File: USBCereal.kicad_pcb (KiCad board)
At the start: 2 copper layers, 24.3 x 19.6 mm, 14 parts, among them J1 USB_C, J2 Conn_01x06, U1 XC6206P332MR, U2 CH340C

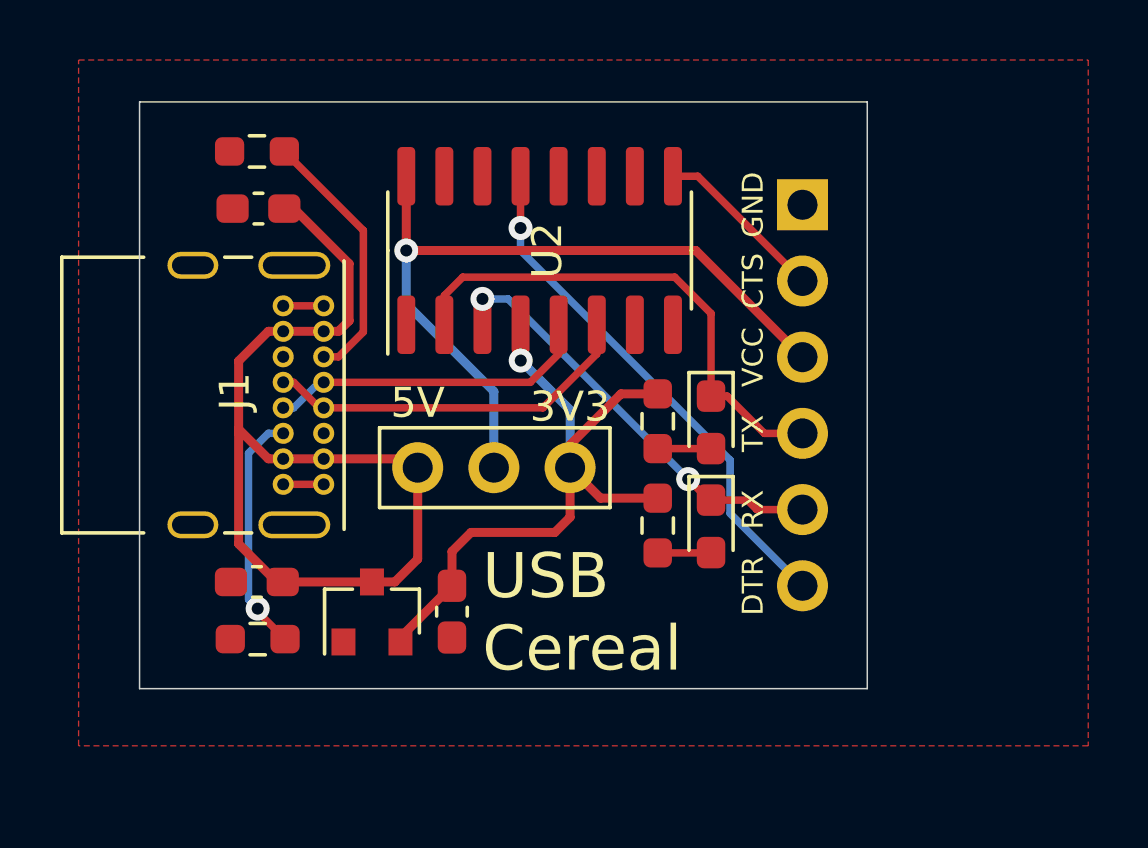
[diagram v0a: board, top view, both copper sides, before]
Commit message: update schematic
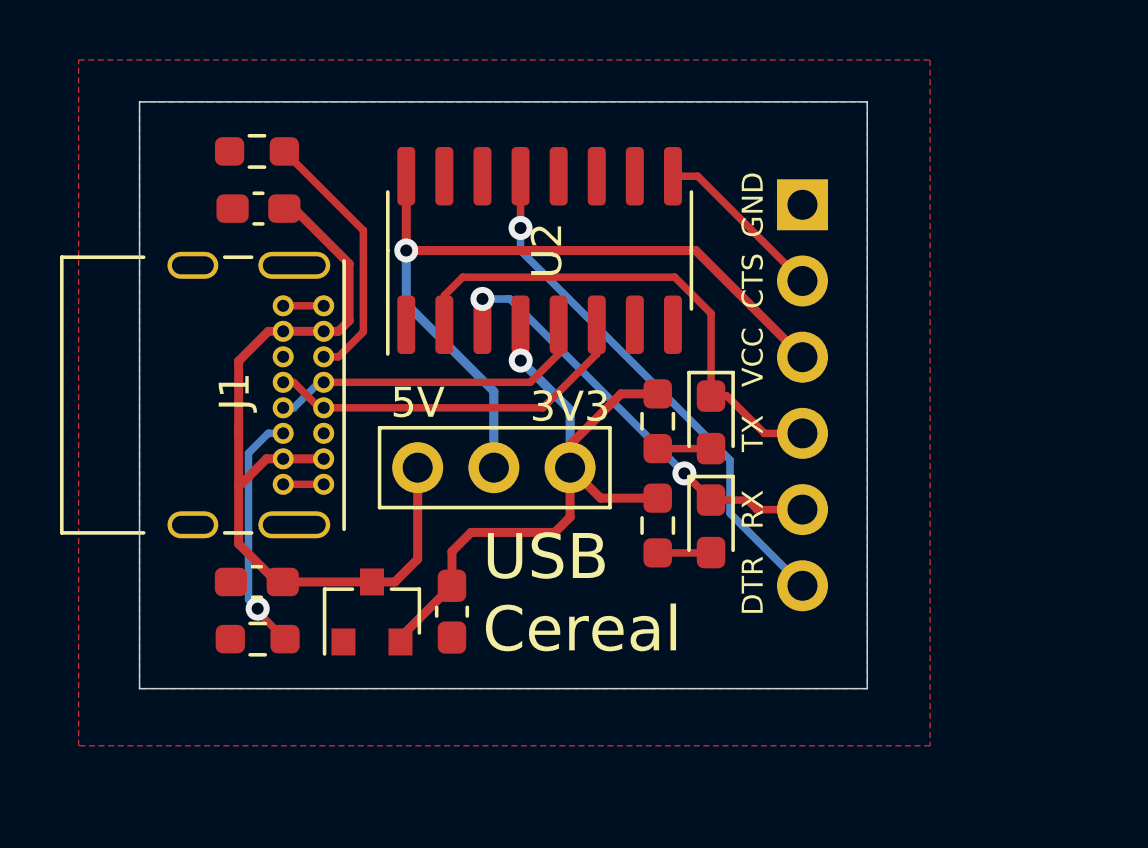
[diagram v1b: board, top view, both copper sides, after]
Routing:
- net +5V: track 31.8 -> 29.0 mm
- added copper zone on B.Cu, net GNDD
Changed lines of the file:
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@@
     (thickness 1.6)
     (drawings 13)
-    (tracks 100)
+    (tracks 102)
     (zones 0)
     (modules 14)
@@
       (effects (font (size 1 1) (thickness 0.15)))
     )
-    (fp_text user %R (at 0 0 90) (layer F.Fab)
-      (effects (font (size 0.4 0.4) (thickness 0.06)))
-    )
     (fp_line (start 0.8 -0.4) (end -0.5 -0.4) (layer F.Fab) (width 0.1))
     (fp_line (start -0.5 -0.4) (end -0.8 -0.1) (layer F.Fab) (width 0.1))
@@
     (fp_line (start 1.65 -0.73) (end 1.65 0.73) (layer F.CrtYd) (width 0.05))
     (fp_line (start 1.65 0.73) (end -1.65 0.73) (layer F.CrtYd) (width 0.05))
+    (fp_text user %R (at 0 0 90) (layer F.Fab)
+      (effects (font (size 0.4 0.4) (thickness 0.06)))
+    )
     (pad 2 smd roundrect (at 0.875 0 270) (size 1.05 0.95) (layers F.Cu F.Paste F.Mask) (roundrect_rratio 0.25)
       (net 13 "Net-(D1-Pad2)"))
@@
     (fp_text value LED_Small (at 4.6485 -0.127 90) (layer F.Fab) hide
       (effects (font (size 1 1) (thickness 0.15)))
-    )
-    (fp_text user %R (at 0 0 90) (layer F.Fab)
-      (effects (font (size 0.4 0.4) (thickness 0.06)))
     )
     (fp_line (start 0.8 -0.4) (end -0.5 -0.4) (layer F.Fab) (width 0.1))
@@
     (fp_line (start 1.65 -0.73) (end 1.65 0.73) (layer F.CrtYd) (width 0.05))
     (fp_line (start 1.65 0.73) (end -1.65 0.73) (layer F.CrtYd) (width 0.05))
+    (fp_text user %R (at 0 0 90) (layer F.Fab)
+      (effects (font (size 0.4 0.4) (thickness 0.06)))
+    )
     (pad 2 smd roundrect (at 0.875 0 270) (size 1.05 0.95) (layers F.Cu F.Paste F.Mask) (roundrect_rratio 0.25)
       (net 14 "Net-(D2-Pad2)"))
@@
     (effects (font (size 0.7 0.7) (thickness 0.1)))
   )
-  (gr_text "USB\nCereal" (at 32.512 34.29) (layer F.SilkS)
+  (gr_text "USB\nCereal" (at 32.512 33.655) (layer F.SilkS)
     (effects (font (size 1.5 1.5) (thickness 0.375)) (justify left))
   )
@@
   (gr_line (start 21.082 36.83) (end 21.082 17.272) (layer Edge.Cuts) (width 0.05))
   (segment (start 25.87 24.919) (end 27.22 24.919) (width 0.3) (layer F.Cu) (net 1))
-  (segment (start 25.375026 29.169) (end 25.87 29.169) (width 0.3) (layer F.Cu) (net 1))
-  (segment (start 24.384 28.177974) (end 25.375026 29.169) (width 0.3) (layer F.Cu) (net 1))
   (segment (start 25.87 29.169) (end 27.22 29.169) (width 0.3) (layer F.Cu) (net 1))
   (segment (start 25.654 33.274) (end 25.855 33.274) (width 0.3) (layer F.Cu) (net 1))
@@
   (segment (start 24.384 25.910026) (end 24.384 28.321) (width 0.3) (layer F.Cu) (net 1))
   (segment (start 25.87 24.919) (end 25.375026 24.919) (width 0.3) (layer F.Cu) (net 1))
-  (segment (start 24.384 28.321) (end 24.384 32.004) (width 0.3) (layer F.Cu) (net 1))
   (segment (start 25.375026 24.919) (end 24.384 25.910026) (width 0.3) (layer F.Cu) (net 1))
   (segment (start 24.384 28.177974) (end 24.384 28.321) (width 0.3) (layer F.Cu) (net 1))
@@
   (segment (start 28.067 24.566974) (end 28.067 22.664616) (width 0.3) (layer F.Cu) (net 1))
   (segment (start 30.058 29.169) (end 30.353 29.464) (width 0.3) (layer F.Cu) (net 1))
-  (segment (start 27.22 29.169) (end 30.058 29.169) (width 0.3) (layer F.Cu) (net 1))
   (segment (start 25.966 33.163) (end 25.855 33.274) (width 0.3) (layer F.Cu) (net 1))
   (segment (start 25.855 33.274) (end 28.829 33.274) (width 0.3) (layer F.Cu) (net 1))
@@
   (segment (start 30.353 32.512) (end 30.353 29.464) (width 0.3) (layer F.Cu) (net 1))
   (segment (start 29.591 33.274) (end 30.353 32.512) (width 0.3) (layer F.Cu) (net 1))
+  (segment (start 25.314 29.169) (end 24.384 30.099) (width 0.3) (layer F.Cu) (net 1))
+  (segment (start 24.384 30.099) (end 24.384 32.004) (width 0.3) (layer F.Cu) (net 1))
+  (segment (start 25.87 29.169) (end 25.314 29.169) (width 0.3) (layer F.Cu) (net 1))
+  (segment (start 24.384 28.321) (end 24.384 30.099) (width 0.3) (layer F.Cu) (net 1))
   (segment (start 25.87 30.019) (end 27.22 30.019) (width 0.25) (layer F.Cu) (net 4))
   (segment (start 25.87 24.069) (end 27.22 24.069) (width 0.25) (layer F.Cu) (net 4))
@@
   (segment (start 41.656 30.861) (end 43.18 30.861) (width 0.25) (layer F.Cu) (net 11))
   (segment (start 41.3395 30.5445) (end 41.656 30.861) (width 0.25) (layer F.Cu) (net 11))
-  (via (at 39.37 29.845) (size 0.8) (drill 0.4) (layers F.Cu B.Cu) (net 11))
-  (segment (start 40.0695 30.5445) (end 39.37 29.845) (width 0.25) (layer F.Cu) (net 11))
+  (via (at 39.243 29.6545) (size 0.8) (drill 0.4) (layers F.Cu B.Cu) (net 11))
   (segment (start 40.132 30.5445) (end 40.0695 30.5445) (width 0.25) (layer F.Cu) (net 11))
   (via (at 32.512 23.839) (size 0.8) (drill 0.4) (layers F.Cu B.Cu) (net 11))
   (segment (start 33.364 23.839) (end 32.512 23.839) (width 0.25) (layer B.Cu) (net 11))
-  (segment (start 39.37 29.845) (end 33.364 23.839) (width 0.25) (layer B.Cu) (net 11))
+  (segment (start 40.132 30.5435) (end 39.243 29.6545) (width 0.25) (layer F.Cu) (net 11))
+  (segment (start 40.132 30.5445) (end 40.132 30.5435) (width 0.25) (layer F.Cu) (net 11))
+  (segment (start 33.4275 23.839) (end 33.364 23.839) (width 0.25) (layer B.Cu) (net 11))
+  (segment (start 39.243 29.6545) (end 33.4275 23.839) (width 0.25) (layer B.Cu) (net 11))
   (segment (start 40.132 27.079) (end 40.668 27.079) (width 0.25) (layer F.Cu) (net 12))
   (segment (start 41.91 28.321) (end 43.18 28.321) (width 0.25) (layer F.Cu) (net 12))
@@
     (connect_pads (clearance 0.0254))
     (min_thickness 0.254)
-    (fill yes (arc_segments 32) (thermal_gap 0.508) (thermal_bridge_width 0.508))
+    (fill yes (arc_segments 32) (thermal_gap 0.3) (thermal_bridge_width 0.3))
     (polygon
       (pts
-        (xy 52.705 38.735) (xy 19.05 38.735) (xy 19.05 15.875) (xy 52.705 15.875)
+        (xy 47.4345 38.735) (xy 19.05 38.735) (xy 19.05 15.875) (xy 47.4345 15.875)
       )
     )
+  )
+  (zone (net 4) (net_name GNDD) (layer B.Cu) (hatch edge 0.508)
+    (connect_pads (clearance 0.0254))
+    (min_thickness 0.254)
+    (fill yes (arc_segments 32) (thermal_gap 0.3) (thermal_bridge_width 0.3))
+    (polygon
+      (pts
+        (xy 45.339 36.83) (xy 21.082 36.83) (xy 21.082 17.272) (xy 45.339 17.272)
+      )
+    )
+  )
+  (zone (net 0) (net_name "") (layer B.Cu) (hatch edge 0.508)
+    (connect_pads (clearance 0.0254))
+    (min_thickness 0.254)
+    (keepout (tracks allowed) (vias allowed) (copperpour not_allowed))
+    (fill (arc_segments 32) (thermal_gap 0.508) (thermal_bridge_width 0.508))
+    (polygon
+      (pts
+        (xy 27.178 30.48) (xy 25.019 30.48) (xy 25.019 28.956) (xy 27.178 28.956)
+      )
+    )
+  )
+  (zone (net 0) (net_name "") (layer F.Cu) (hatch edge 0.508)
+    (connect_pads (clearance 0.0254))
+    (min_thickness 0.254)
+    (keepout (tracks allowed) (vias allowed) (copperpour not_allowed))
+    (fill (arc_segments 32) (thermal_gap 0.508) (thermal_bridge_width 0.508))
+    (polygon
+      (pts
+        (xy 31.877 22.86) (xy 30.988 23.6855) (xy 30.6705 23.6855) (xy 30.1625 23.495) (xy 30.1625 22.5425)
+        (xy 31.877 22.5425)
+      )
+    )
+  )
+  (zone (net 0) (net_name "") (layer F.Cu) (hatch edge 0.508)
+    (connect_pads (clearance 0.0254))
+    (min_thickness 0.254)
+    (keepout (tracks allowed) (vias allowed) (copperpour not_allowed))
+    (fill (arc_segments 32) (thermal_gap 0.508) (thermal_bridge_width 0.508))
+    (polygon
+      (pts
+        (xy 30.48 26.3525) (xy 27.7495 26.3525) (xy 27.7495 25.9715) (xy 28.829 24.892) (xy 30.48 24.892)
+      )
+    )
+  )
+  (zone (net 0) (net_name "") (layer B.Cu) (hatch edge 0.508)
+    (connect_pads (clearance 0.0254))
+    (min_thickness 0.254)
+    (keepout (tracks allowed) (vias allowed) (copperpour not_allowed))
+    (fill (arc_segments 32) (thermal_gap 0.3) (thermal_bridge_width 0.3))
+    (polygon
+      (pts
+        (xy 27.1145 24.1935) (xy 25.908 24.1935) (xy 25.908 23.241) (xy 27.1145 23.241)
+      )
+    )
+  )
+  (zone (net 0) (net_name "") (layer F.Cu) (hatch edge 0.508)
+    (connect_pads (clearance 0.0254))
+    (min_thickness 0.254)
+    (keepout (tracks allowed) (vias allowed) (copperpour not_allowed))
+    (fill (arc_segments 32) (thermal_gap 0.3) (thermal_bridge_width 0.3))
+    (polygon
+      (pts
+        (xy 27.2415 30.861) (xy 24.8285 30.861) (xy 24.8285 29.9085) (xy 27.2415 29.9085)
+      )
+    )
+  )
+  (zone (net 0) (net_name "") (layer F.Cu) (hatch edge 0.508)
+    (connect_pads (clearance 0.0254))
+    (min_thickness 0.254)
+    (keepout (tracks allowed) (vias allowed) (copperpour not_allowed))
+    (fill (arc_segments 32) (thermal_gap 0.3) (thermal_bridge_width 0.3))
+    (polygon
+      (pts
+        (xy 27.3685 24.257) (xy 25.9715 24.257) (xy 25.9715 23.368) (xy 27.3685 23.368)
+      )
+    )

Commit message: Add logo
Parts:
- added G***: LOGO, USBCereal:USBCereal, B.Cu at (37.4, 23.6)

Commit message: Finished PCB, generated fabrication files
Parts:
- added REF**: JLCPCB_Tooling_Hole, USBCereal:JLCPCB_Tooling_Hole, F.Cu at (45.3, 27.1)
- added REF**: JLCPCB_Tooling_Hole, USBCereal:JLCPCB_Tooling_Hole, F.Cu at (22.0, 34.2)
- added REF**: JLCPCB_Tooling_Hole, USBCereal:JLCPCB_Tooling_Hole, F.Cu at (22.0, 19.9)
- J1: footprint Connector_USB:USB_C_Receptacle_GCT_USB4085 -> Connector_USB:USB_C_Receptacle_HRO_TYPE-C-31-M-12
- R3, R4: value 51 -> 47R
- moved J1 4.58 mm to (23.7, 27.1)
- moved R2 1.91 mm to (25.1, 20.8)
- moved R1 1.88 mm to (25.1, 33.3)
- moved C2 1.78 mm to (25.1, 35.1)
- moved C1 1.78 mm to (25.1, 19.1)
- moved G*** 1.76 mm to (35.8, 22.9)
- moved D1 0.76 mm to (40.9, 28.0)
- moved D2 0.76 mm to (40.9, 31.4)
- moved R3 0.76 mm to (39.1, 27.9)
- moved R4 0.76 mm to (39.1, 31.4)
- moved U2 0.76 mm to (35.2, 22.2)
- moved JP1 0.76 mm to (31.1, 29.5)
- moved C3 0.13 mm to (31.6, 34.3)
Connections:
- J1 pad A8: Net-(J1-PadA8) -> (no net)
- J1 pad B8: Net-(J1-PadB8) -> (no net)
- U2 pad 10: Net-(U2-Pad10) -> (no net)
- U2 pad 11: Net-(U2-Pad11) -> (no net)
- U2 pad 12: Net-(U2-Pad12) -> (no net)
- U2 pad 14: Net-(U2-Pad14) -> (no net)
- U2 pad 15: Net-(U2-Pad15) -> (no net)
- U2 pad 7: Net-(U2-Pad7) -> (no net)
- U2 pad 8: Net-(U2-Pad8) -> (no net)
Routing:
- net /USB_D-: track 12.5 -> 16.2 mm, vias 0 -> 2
- net /USB_D+: track 10.9 -> 13.0 mm
- net /CC1: track 8.77 -> 6.78 mm
- net +5V: track 29.0 -> 27.1 mm, vias 0 -> 3
- net /CC2: track 8.13 -> 6.42 mm, vias 1 -> 0
- net GNDD: track 2.70 -> 4.34 mm, vias 0 -> 8
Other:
- board size 24.3 x 19.6 mm -> 25.1 x 19.6 mm
- net class VCC: trace_width 0.3 -> 0.5
- board text added: "JLCJLCJLCJLC"

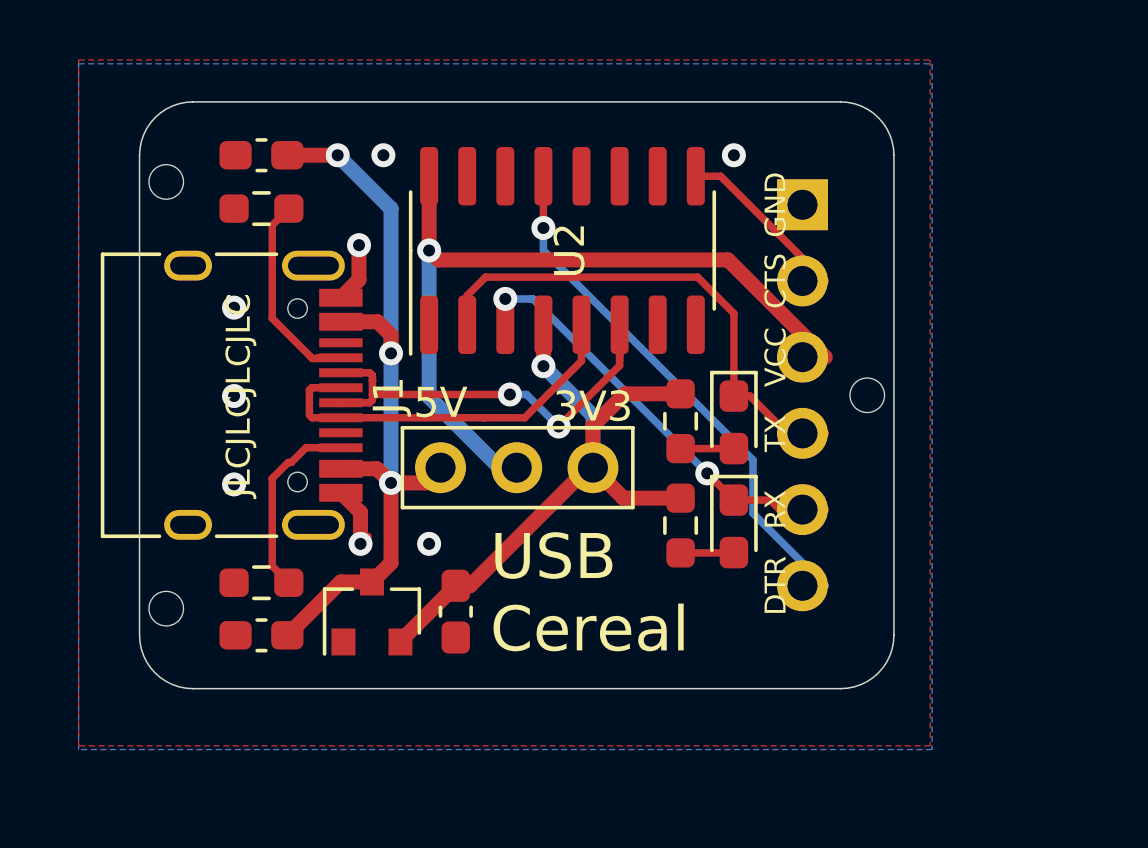
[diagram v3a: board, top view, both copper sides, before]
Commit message: update non-connecting traces, rebuild gerber's
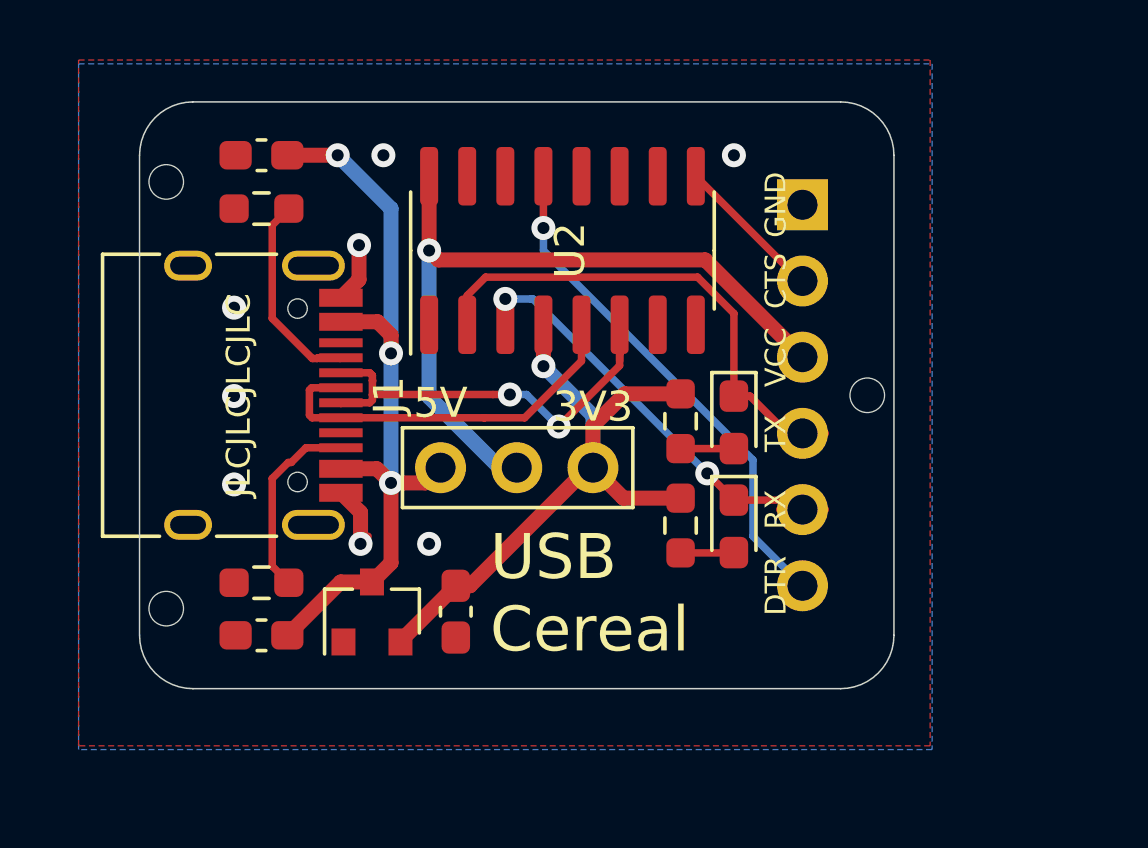
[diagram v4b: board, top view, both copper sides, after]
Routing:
- net VCC: track 25.9 -> 25.2 mm
- net /RXD: track 13.6 -> 14.4 mm
- net /CTS: track 5.76 -> 5.00 mm

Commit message: fixed silk screen issue and updated gerbers
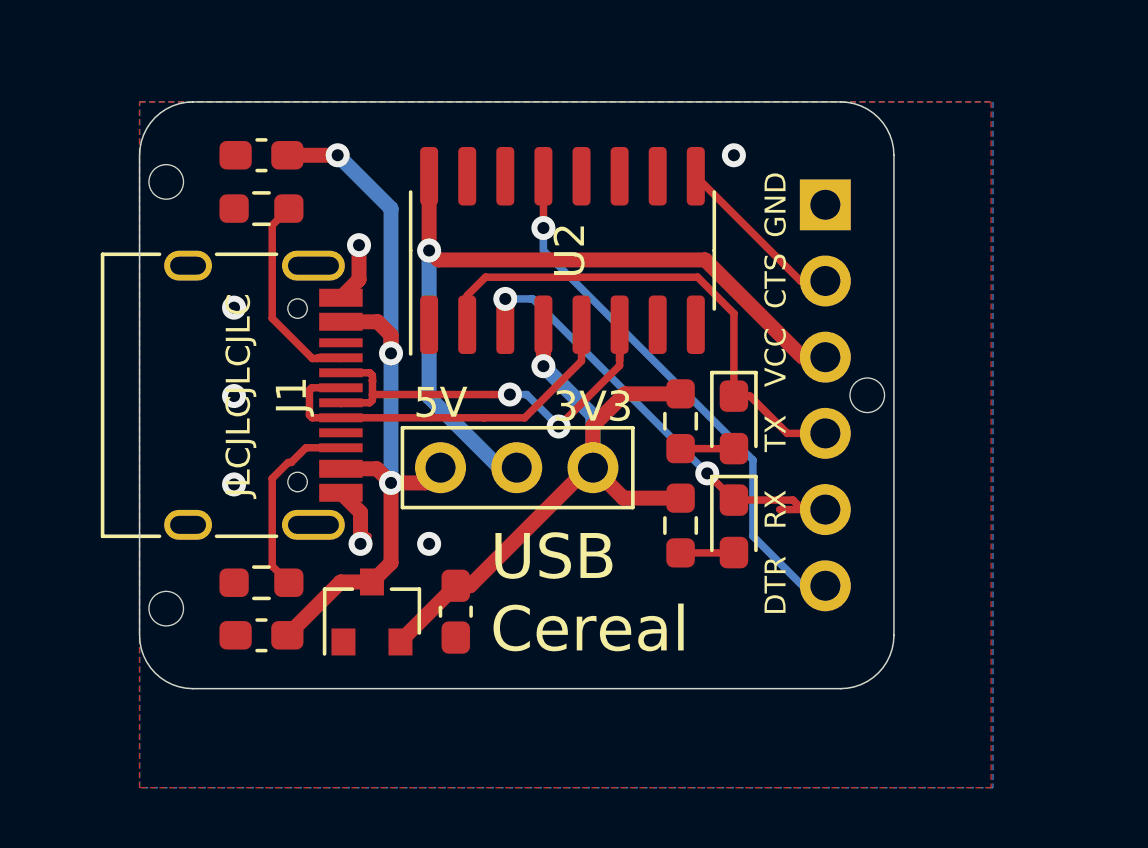
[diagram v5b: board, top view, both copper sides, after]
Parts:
- moved J2 0.76 mm to (43.9, 20.7)
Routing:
- net GNDD: vias 8 -> 7
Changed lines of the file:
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@@
     (thickness 1.6)
     (drawings 19)
-    (tracks 135)
+    (tracks 134)
     (zones 0)
     (modules 18)
@@
     (tags "usb usb-c 2.0 pd")
     (attr smd)
-    (fp_text reference J1 (at 0 -5.645 90) (layer F.SilkS)
+    (fp_text reference J1 (at 0 -2.413 90) (layer F.SilkS)
       (effects (font (size 1 1) (thickness 0.15)))
     )
@@
   )
   (module Connector_PinHeader_2.54mm:PinHeader_1x06_P2.54mm_Horizontal (layer F.Cu)
-    (at 43.18 20.701)
+    (at 43.942 20.701)
     (descr "Through hole angled pin header, 1x06, 2.54mm pitch, 6mm pin length, single row")
     (tags "Through hole angled pin header THT 1x06 2.54mm single row")
@@
   (via (at 24.2316 27.0764) (size 0.8) (drill 0.4) (layers F.Cu B.Cu) (net 2))
   (via (at 40.894 19.05) (size 0.8) (drill 0.4) (layers F.Cu B.Cu) (net 2))
-  (via (at 29.21 19.05) (size 0.8) (drill 0.4) (layers F.Cu B.Cu) (net 2))
   (via (at 30.734 32.004) (size 0.8) (drill 0.4) (layers F.Cu B.Cu) (net 2))
   (segment (start 34.549847 24.705847) (end 34.544 24.7) (width 0.3) (layer F.Cu) (net 3))
@@
     (polygon
       (pts
-        (xy 47.4345 38.735) (xy 19.05 38.735) (xy 19.05 15.875) (xy 47.4345 15.875)
+        (xy 49.4665 40.132) (xy 21.082 40.132) (xy 21.082 17.272) (xy 49.4665 17.272)
       )
     )
@@
     (polygon
       (pts
-        (xy 47.498 38.862) (xy 19.05 38.862) (xy 19.05 16.002) (xy 47.498 16.002)
+        (xy 49.53 40.132) (xy 21.082 40.132) (xy 21.082 17.272) (xy 49.53 17.272)
       )
     )
